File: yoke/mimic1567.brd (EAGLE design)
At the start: 160 x 100 mm, 62 parts, among them J15 JST-VH-5, P1 25 K, P2 10 K, P4 20 K, P5 200, P6 44PINEDGE, Q1 2N3904, Q10 2N2907, Q12 2N3906, Q2 2N3904, Q3 2N3904, Q4 2N3904, Q5 2N3904, Q6 2N3904, Q7 2N3904, Q8 2N2907, Q9 2N3906

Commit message: update netlist
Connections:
- removed net +10V: P6.A
- removed net +5V: P6.F
- removed net -15V: P6.C
- net +50V: now also P6.M; no longer P6.E
- net -10V: now also P6.E
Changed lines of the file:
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@@
 <contactref element="C7" pad="1"/>
 <contactref element="C5" pad="1"/>
+<contactref element="P6" pad="E"/>
 <wire x1="-22.17" y1="113.03" x2="-19.05" y2="124.46" width="0" layer="19" extent="1-1"/>
 <wire x1="-34.29" y1="124.46" x2="-19.05" y2="124.46" width="0" layer="19" extent="1-1"/>
@@
 <wire x1="-54.23" y1="78.74" x2="-35.18" y2="78.74" width="0" layer="19" extent="1-1"/>
 <wire x1="-57.09" y1="66.04" x2="-54.23" y2="78.74" width="0" layer="19" extent="1-1"/>
+<wire x1="-94.3356" y1="50.546" x2="-57.09" y2="66.04" width="0" layer="19" extent="16-16"/>
 <wire x1="-86.86" y1="102.87" x2="-54.23" y2="78.74" width="0" layer="19" extent="1-1"/>
 <wire x1="-103.37" y1="102.87" x2="-86.86" y2="102.87" width="0" layer="19" extent="1-1"/>
@@
 <wire x1="-174.57" y1="-114.3" x2="-181.72" y2="-4.72" width="0" layer="19" extent="1-1"/>
 </signal>
-<signal name="-15V">
-<contactref element="P6" pad="C"/>
-</signal>
-<signal name="+5V">
-<contactref element="P6" pad="F"/>
-</signal>
-<signal name="+10V">
-<contactref element="P6" pad="A"/>
-</signal>
 <signal name="+50V">
-<contactref element="P6" pad="E"/>
 <contactref element="R2" pad="1"/>
 <contactref element="R6" pad="1"/>
 <contactref element="R9" pad="1"/>
 <contactref element="R3" pad="1"/>
+<contactref element="P6" pad="M"/>
+<wire x1="-70.5612" y1="50.546" x2="-100.19" y2="-36.83" width="0" layer="19" extent="16-16"/>
+<wire x1="-65.54" y1="102.87" x2="-70.5612" y2="50.546" width="0" layer="19" extent="16-16"/>
+<wire x1="-82.05" y1="102.87" x2="-65.54" y2="102.87" width="0" layer="19" extent="1-1"/>
 <wire x1="81.42" y1="-106.68" x2="-100.19" y2="-36.83" width="0" layer="19" extent="1-1"/>
-<wire x1="-94.3356" y1="50.546" x2="-100.19" y2="-36.83" width="0" layer="19" extent="16-16"/>
-<wire x1="-82.05" y1="102.87" x2="-94.3356" y2="50.546" width="0" layer="19" extent="16-16"/>
-<wire x1="-65.54" y1="102.87" x2="-82.05" y2="102.87" width="0" layer="19" extent="1-1"/>
 </signal>
 <signal name="N$6">

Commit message: preamplifier card being routed
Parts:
- removed C7: 0.022 uF, keiths:CAP-ZERO-PT-ZERO-22UF-250V-FILM
- removed J15: JST-VH-5, keiths:VHR-5N
- removed P6: 44PINEDGE, keiths:44PINEDGE
- removed Q12: 2N3906, keiths:TO92
- removed R26: 274 K 1%, keiths:R_QUARTERWATT
- added C2: 0.022 uF, keiths:CAP-ZERO-PT-ZERO-22UF-250V-FILM
- added J1: JST-VH-5, keiths:VHR-5N
- added P3: 10 K, keiths:3006P
- added Q11: 2N2907, keiths:TO18
- added R25: 330, keiths:R_ONEWATT
- added R5: 10K, keiths:R_QUARTERWATT
- added R8: 25K, keiths:R_QUARTERWATT
- C1: value 3.3UF 5% -> 3.3uF
- C3, C6: value 0.022 uF -> 0.022uF
- C4: value 3.3UF 5% -> 0.022uF; device keiths:CAP-3-PT-ZERO-3UF-250V-FILM -> keiths:CAP-ZERO-PT-ZERO-22UF-250V-FILM
- C5: value 0.022 uF -> 3.3uF; device keiths:CAP-ZERO-PT-ZERO-22UF-250V-FILM -> keiths:CAP-3-PT-ZERO-3UF-250V-FILM
- P1: value 25 K -> 20K
- P2: value 10 K -> 25 K
- P4: value 20 K -> 200
- P5: value 200 -> 44PINEDGE; device keiths:3006P -> keiths:44PINEDGE
- Q10: value 2N2907 -> 2N3904; device keiths:TO18 -> keiths:TO92
- Q4: value 2N3904 -> 2N2907; device keiths:TO92 -> keiths:TO18
- Q5: value 2N3904 -> 2N3906
- Q8: value 2N2907 -> 2N3906; device keiths:TO18 -> keiths:TO92
- Q9: value 2N3906 -> 2N3904
- R1: value 3.3uF -> 274K; device keiths:R_THREEWATT -> keiths:R_QUARTERWATT
- R10: value 33.2 K 1% -> 274K; device keiths:R_HALFWATT -> keiths:R_QUARTERWATT
- R11: value 4.64K -> 6.81K 1%; device keiths:R_QUARTERWATT -> keiths:R_HALFWATT
- R12: value 2.94K -> 33.2K; device keiths:R_QUARTERWATT -> keiths:R_HALFWATT
- R13: value 3.3 -> 2K; device keiths:R_THREEWATT -> keiths:R_QUARTERWATT
- R14: value 1.96 K 1 % -> 10K; device keiths:R_QUARTERWATT -> keiths:R_HALFWATT
- R15: value 330 5% -> 3.3K; device keiths:R_ONEWATT -> keiths:R_TWOWATT
- R16: value 10 K 5% -> 6.81K
- R17: value 274 K 1% -> 33.2K; device keiths:R_QUARTERWATT -> keiths:R_HALFWATT
- R18: value 1.96 K 1 % -> 2K
- R19: value 1 K 1% -> 10K; device keiths:R_QUARTERWATT -> keiths:R_HALFWATT
- R2: value 3.3K 5% -> 137; device keiths:R_TWOWATT -> keiths:R_QUARTERWATT
- R20: value 137 1% -> 3.3K; device keiths:R_QUARTERWATT -> keiths:R_TWOWATT
- R21: value 1 K 1% -> 3.3; device keiths:R_QUARTERWATT -> keiths:R_THREEWATT
- R22: value 330 5% -> 1K; device keiths:R_ONEWATT -> keiths:R_QUARTERWATT
- R23: value 2 K 1% -> 1K
- R24: value 2 K 1% -> 330; device keiths:R_QUARTERWATT -> keiths:R_ONEWATT
- R3: value 3.3K 5% -> 1.96K; device keiths:R_TWOWATT -> keiths:R_QUARTERWATT
- R4: value 10 K 5% -> 10K; device keiths:R_HALFWATT -> keiths:R_QUARTERWATT
- R6: value 6.81K 1% -> 1.96K; device keiths:R_HALFWATT -> keiths:R_QUARTERWATT
- R7: value 33.2 K 1% -> 25K; device keiths:R_HALFWATT -> keiths:R_QUARTERWATT
- R9: value 6.81K 1% -> 3.3uF; device keiths:R_HALFWATT -> keiths:R_THREEWATT
- moved R21 336.2 mm to (143.5, 33.8), turned to 90 degrees
- moved R14 324.2 mm to (95.2, 58.4), turned to 270 degrees
- moved P4 323.3 mm to (110.5, 101.6), turned to 90 degrees
- moved R19 320.4 mm to (95.2, 41.1), turned to 90 degrees
- moved R24 303.9 mm to (120.7, 22.4), turned to 270 degrees
- moved R23 253.1 mm to (19.1, 22.9), turned to 90 degrees
- moved R2 243.6 mm to (118.1, 87.4), turned to 270 degrees
- moved R20 236.5 mm to (133.3, 22.4), turned to 270 degrees
- moved C3 232.5 mm to (108.0, 55.9), turned to 90 degrees
- moved D7 221.1 mm to (133.3, 65.5), turned to 90 degrees
- moved R9 220.3 mm to (143.5, 86.6), turned to 270 degrees
- moved C1 218.5 mm to (156.2, 87.6)
- moved P5 217.9 mm to (0.00, 57.1), turned to 270 degrees
- moved D2 213.2 mm to (82.5, 82.5), turned to 270 degrees
- moved Q1 208.3 mm to (72.1, 66.0), turned to 45 degrees
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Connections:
- removed net N$13 (its old number): D11.A, D12.C
- removed net N$23: Q5.3
- new net N$37: D12.C, D13.A
- net +50V: now also P5.M, R11.1, R15.1, R16.1, R20.1; no longer P6.M, R2.1, R3.1, R6.1, R9.1
- net -10V: now also C3.1, C4.1, P5.E, Q1.1, Q2.1, Q3.1, Q6.1, Q9.1, R14.2, R19.2, R24.2, R25.2, R6.2; no longer C5.1, C7.1, P6.E, Q1.3, Q2.3, Q4.3, Q6.3, R15.2, R16.2, R18.2, R22.2, R4.2
- net GND: now also J1.P$5, P3.2, P3.3, P5.D, R21.2, R3.2, R4.1, R5.1, R7.1, R8.1, R9.2; no longer J15.P$5, P1.2, P1.3, P6.D, R1.2, R11.1, R12.1, R13.2, R14.2
- net N$10: now also D2.C, D6.A; no longer D14.A, D15.C
- net N$11: now also D1.C, D2.A; no longer D13.A, D14.C
- net N$12: now also D1.A, D4.C; no longer D12.A, D13.C
- net N$14: now also D3.C, D5.A; no longer D10.A, D11.C
- net N$15: now also C2.1, D3.A, Q5.3; no longer C3.1, D10.C, Q9.3
- net N$16: now also Q5.2, Q7.3, R12.2; no longer Q3.1, Q9.2, R7.2
- net N$17: now also R11.2, R12.1; no longer R7.1, R9.2
- net N$19: now also Q1.3, Q10.1, Q7.1; no longer Q3.3, Q5.1, Q7.3
- net N$2: now also J1.P$4, R13.2; no longer J15.P$4, R24.2
- net N$20: now also R16.2, R17.1; no longer R10.1, R6.2
- net N$21: now also Q5.1, Q9.3; no longer Q2.1, Q9.1
- net N$22: now also P4.1, R10.1, R2.2, R3.1; no longer P5.1, R14.1, R20.2, R26.1
- net N$25: now also Q10.3, Q8.2, R17.2; no longer Q12.2, Q7.1, R10.2
- net N$27: now also C5.1, J1.P$2, R18.1; no longer C4.1, J15.P$2, R23.1
- net N$29: now also P3.1, Q1.2, Q2.2, Q2.3, R4.2, R5.2; no longer P2.1, Q5.2, Q6.1, Q6.2, R11.2, R12.2
- net N$3: now also R9.1; no longer R1.1
- net N$30: now also C5.2, R21.1; no longer C4.2, R13.1
- net N$31: now also D16.C, J1.P$1, Q11.1, R20.2; no longer D2.C, J15.P$1, Q10.1, R3.2
- net N$33: now also D15.C, D16.A, Q11.2, R19.1; no longer D1.C, D2.A, Q10.2, R16.1
- net N$34: now also C4.2, Q11.3, R24.1; no longer C7.2, Q10.3, R15.1
- net N$35: now also D14.C, D15.A; no longer D1.A, D3.C
- net N$36: now also D13.C, D14.A; no longer D3.A, D4.C
- net N$38: now also D11.C, D12.A; no longer D5.A, D6.C
- net N$39: now also D10.C, D11.A; no longer D6.A, D7.C
- net N$4: now also P2.1, Q3.2, Q6.2, Q6.3, Q9.2, R7.2, R8.2; no longer P1.1, Q1.1, Q1.2, Q2.2, Q4.2
- net N$40: now also D10.A, Q8.3; no longer D7.A, Q12.3
- net N$43: now also Q10.2, R18.2, R22.2; no longer Q7.2, R21.2, R23.2
- net N$44: now also P4.3, R1.1, R2.1, R6.1; no longer P5.3, R17.1, R18.1, R20.1
- net N$5: now also D7.C, J1.P$3, Q4.1, R15.2; no longer D16.A, J15.P$3, Q8.1, R2.2
- net N$6: now also Q7.2, R13.1, R23.2; no longer Q3.2, R19.2, R24.1
- net N$7: now also C2.2, D6.C, D7.A, Q4.2, R14.1; no longer C3.2, D15.A, D16.C, Q8.2, R4.1
- net N$8: now also C3.2, Q4.3, R25.1; no longer C5.2, Q8.3, R22.1
- net N$9: now also Q3.3, Q8.1; no longer Q12.1, Q4.1
- net W_IN: now also P1.2, P1.3, P5.W, R1.2, R10.2, R22.1; no longer P4.3, P5.2, P6.W, R17.2, R21.1, R26.2
- net Z_IN: now also P1.1, P5.Z, R23.1; no longer P4.1, P6.Z, R19.1
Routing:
- net -10V: track 0.00 -> 252.0 mm
- net GND: track 0.00 -> 241.7 mm
- net W_IN: track 0.00 -> 186.4 mm
- net +50V: track 0.00 -> 166.2 mm
- net N$27: track 0.00 -> 103.5 mm
- net Z_IN: track 0.00 -> 95.3 mm
- net N$6: track 0.00 -> 94.0 mm
- net N$4: track 0.00 -> 84.7 mm
- net N$2: track 0.00 -> 83.2 mm
- net N$15: track 0.00 -> 83.0 mm
- net N$43: track 0.00 -> 79.3 mm
- net N$33: track 0.00 -> 66.8 mm
- net N$31: track 0.00 -> 63.5 mm
- net N$40: track 0.00 -> 62.4 mm
- net N$29: track 0.00 -> 61.2 mm
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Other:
- board size 160 x 100 mm -> 165.1 x 114.3 mm

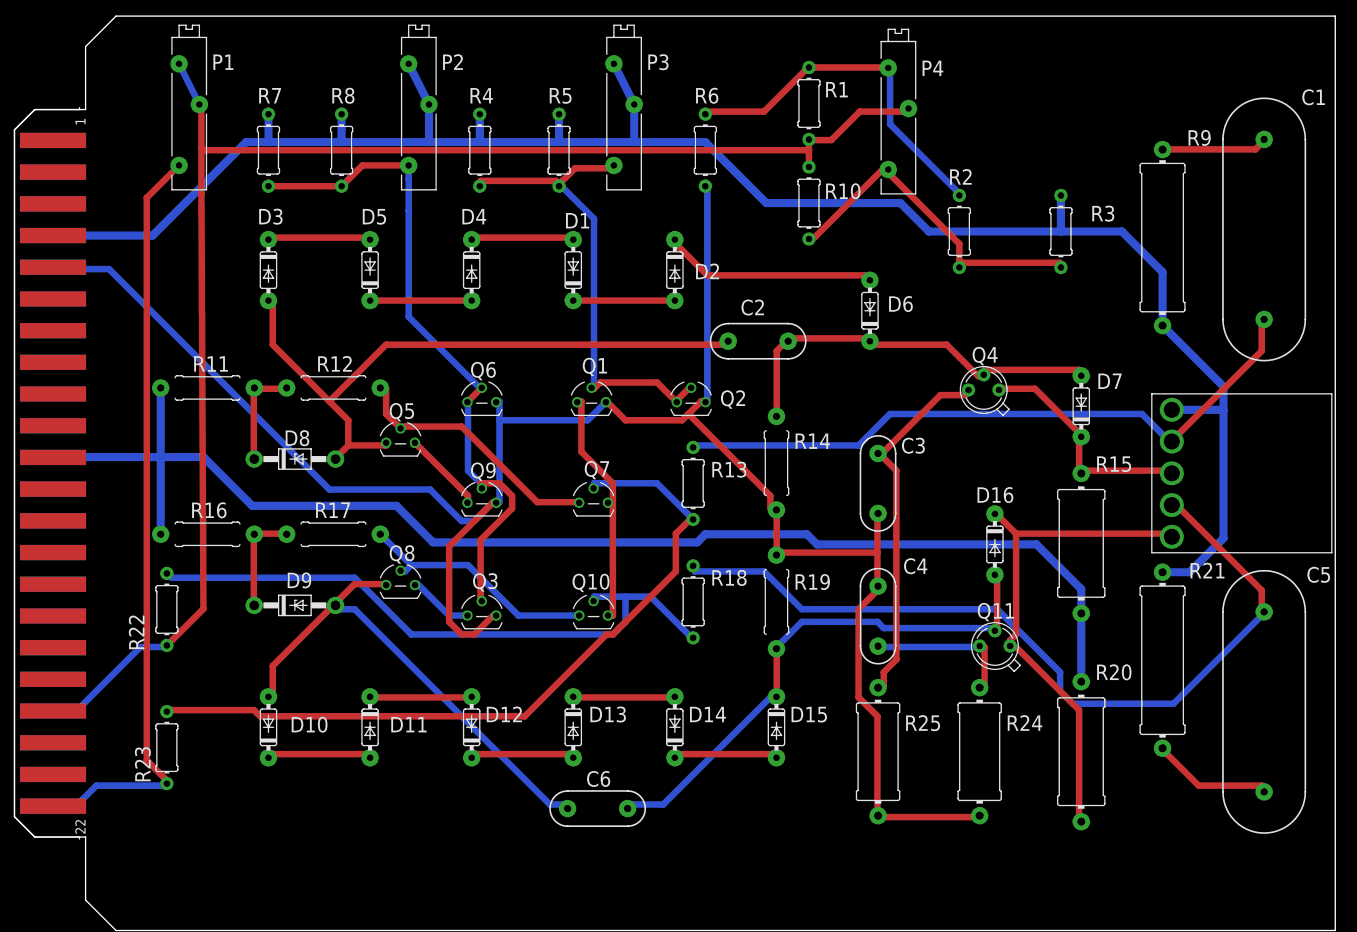
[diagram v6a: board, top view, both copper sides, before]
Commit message: D/A being routed
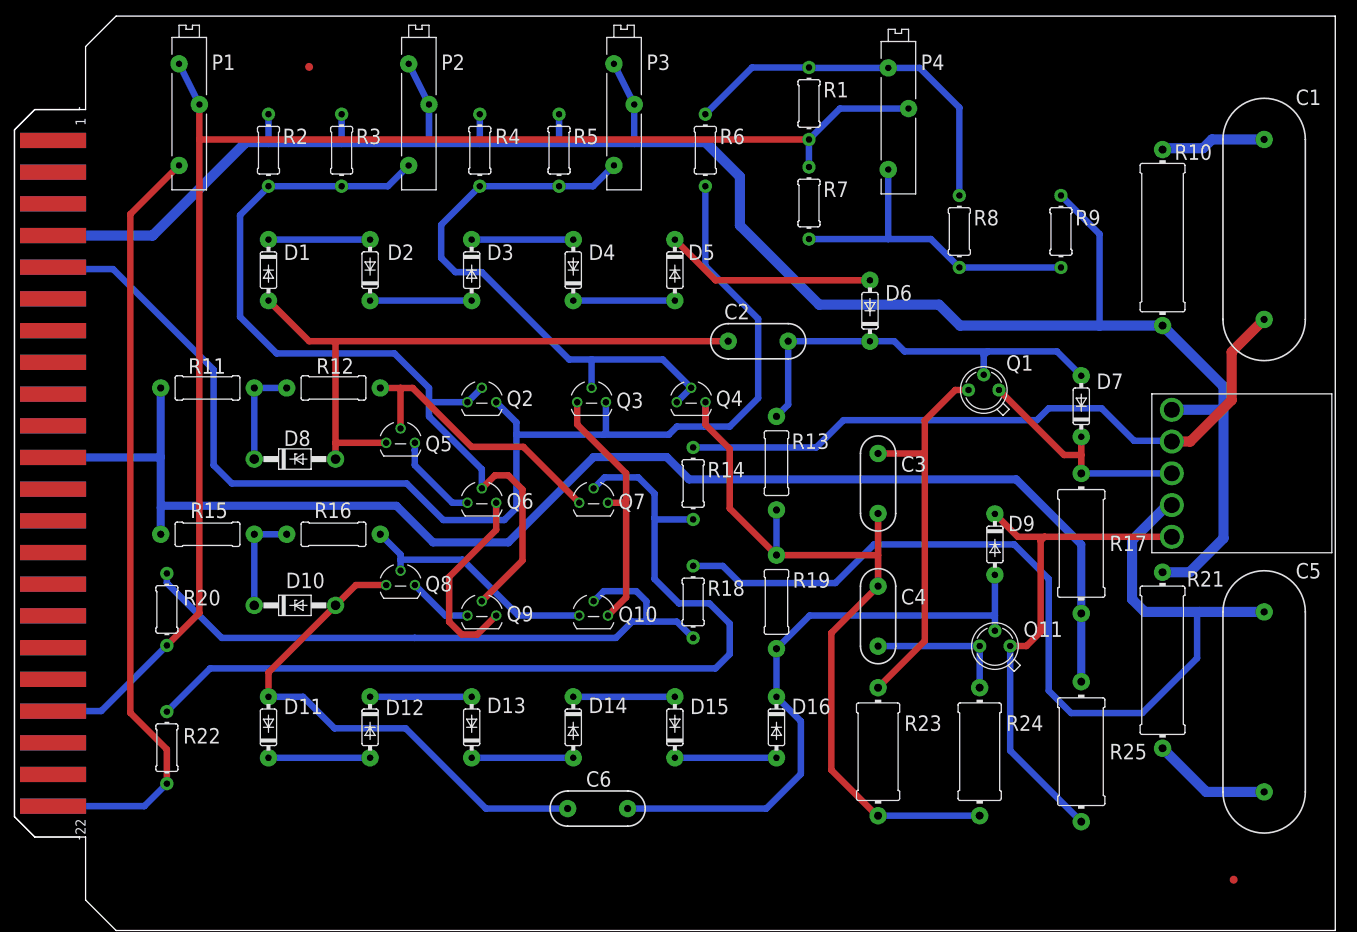
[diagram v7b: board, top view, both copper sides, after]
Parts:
- added U$1, U$2: FIDUCIAL, adafruit:FIDUCIAL_1MM
- D10: value 1N4148 -> 1N4736A; device keiths:DO35-7 -> keiths:DO41
- D9: value 1N4736A -> 1N4148; device keiths:DO41 -> keiths:DO35-7
- Q1: value 2N3904 -> 2N2907; device keiths:TO92 -> keiths:TO18
- Q4: value 2N2907 -> 2N3904; device keiths:TO18 -> keiths:TO92
- R10: value 274K -> 3.3uF; device keiths:R_QUARTERWATT -> keiths:R_THREEWATT
- R11: value 6.81K 1% -> 6.81K
- R13: value 2K -> 10K; device keiths:R_QUARTERWATT -> keiths:R_HALFWATT
- R14: value 10K -> 2K; device keiths:R_HALFWATT -> keiths:R_QUARTERWATT
- R15: value 3.3K -> 6.81K; device keiths:R_TWOWATT -> keiths:R_HALFWATT
- R16: value 6.81K -> 33.2K
- R17: value 33.2K -> 3.3K; device keiths:R_HALFWATT -> keiths:R_TWOWATT
- R2: value 137 -> 25K
- R20: value 3.3K -> 1K; device keiths:R_TWOWATT -> keiths:R_QUARTERWATT
- R23: value 1K -> 330; device keiths:R_QUARTERWATT -> keiths:R_ONEWATT
- R25: value 330 -> 3.3K; device keiths:R_ONEWATT -> keiths:R_TWOWATT
- R3: value 1.96K -> 25K
- R7: value 25K -> 274K
- R8: value 25K -> 137
- R9: value 3.3uF -> 1.96K; device keiths:R_THREEWATT -> keiths:R_QUARTERWATT
- moved R20 115.7 mm to (19.1, 40.1), turned to 90 degrees
- moved R15 109.2 mm to (24.1, 49.5), turned to 0 degrees
- moved R17 93.5 mm to (133.3, 48.4), turned to 90 degrees
- moved R3 90.5 mm to (40.9, 97.5), turned to 270 degrees
- moved R23 88.9 mm to (108.0, 22.4), turned to 270 degrees
- moved D9 87.8 mm to (122.6, 48.3), turned to 270 degrees
- moved R2 87.0 mm to (31.8, 97.5)
- moved R8 77.9 mm to (118.1, 87.4)
- moved R7 67.9 mm to (99.3, 90.9), turned to 90 degrees
- moved Q1 49.0 mm to (121.2, 67.6), turned to 0 degrees
- moved R10 44.4 mm to (143.5, 86.6), turned to 270 degrees
- moved D1 38.1 mm to (31.8, 82.5), turned to 270 degrees
- moved D2 38.1 mm to (44.5, 82.5), turned to 90 degrees
- moved D5 38.1 mm to (82.5, 82.5), turned to 270 degrees
- moved Q4 36.6 mm to (84.6, 66.0), turned to 45 degrees
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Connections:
- removed net N$14 (its old number): D3.C, D5.A
- removed net N$39 (its old number): D10.C, D11.A
- new net N$11: D4.C, D5.A
- new net N$35: D15.C, D16.A
- net +50V: now also R17.1, R25.1; no longer R16.1, R20.1
- net -10V: now also Q4.1, R13.2, R23.2; no longer Q1.1, R14.2, R25.2
- net GND: now also R10.2, R2.1, R3.1; no longer R3.2, R7.1, R8.1
- net N$10: now also D5.C; no longer D2.C
- net N$12: now also D3.C, D4.A; no longer D1.A, D4.C
- net N$13: now also D2.C, D3.A; no longer D4.A, D5.C
- net N$15: now also D1.A; no longer D3.A
- net N$19: now also Q3.3; no longer Q1.3
- net N$2: now also R14.2; no longer R13.2
- net N$20: now also D10.C, R15.2, R16.1; no longer D9.C, R16.2, R17.1
- net N$21: now also Q6.3; no longer Q9.3
- net N$22: now also R7.1, R8.2, R9.1; no longer R10.1, R2.2, R3.1
- net N$25: now also R16.2; no longer R17.2
- net N$29: now also Q3.2, Q4.2, Q4.3; no longer Q1.2, Q2.2, Q2.3
- net N$3: now also R10.1; no longer R9.1
- net N$31: now also D9.C, R25.2; no longer D16.C, R20.2
- net N$33: now also D16.C, D9.A; no longer D15.C, D16.A
- net N$4: now also Q2.2, Q2.3, R2.2, R3.2; no longer Q3.2, Q6.3, R7.2, R8.2
- net N$40: now also D11.A; no longer D9.A
- net N$43: now also R20.2; no longer R22.2
- net N$44: now also R8.1; no longer R2.1
- net N$5: now also Q1.1, R17.2; no longer Q4.1, R15.2
- net N$6: now also R14.1, R22.2; no longer R13.1, R23.2
- net N$7: now also Q1.2, R13.1; no longer Q4.2, R14.1
- net N$8: now also Q1.3, R23.1; no longer Q4.3, R25.1
- net N$9: now also Q9.3; no longer Q3.3
- net W_IN: now also R20.1, R7.2; no longer R10.2, R22.1
- net Z_IN: now also R22.1; no longer R23.1
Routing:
- net -10V: track 252.0 -> 284.9 mm
- net N$4: track 84.7 -> 108.9 mm
- net N$27: track 103.5 -> 123.4 mm
- net N$6: track 94.0 -> 113.5 mm
- net GND: track 241.7 -> 255.2 mm
- net N$39 (its old number): track 13.1 -> 0.00 mm
- net N$14 (its old number): track 12.8 -> 0.00 mm
- net N$35: track 0.00 -> 12.7 mm
- net N$11: track 0.00 -> 12.7 mm
- net N$29: track 61.2 -> 72.8 mm
- net N$33: track 66.8 -> 76.4 mm
- net +50V: track 166.2 -> 174.9 mm
- net N$16: track 32.7 -> 35.9 mm
- net N$40: track 62.4 -> 65.5 mm
- net N$8: track 46.0 -> 48.7 mm
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
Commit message: end of day
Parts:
- added R26, R27: 1.2K, keiths:R_FIVEWATT
- added R28: 1K, keiths:R_QUARTERWATT
- added R29, R30: 330, keiths:R_ONEWATT
- C2: value 0.022 uF -> 3.3uF; device keiths:CAP-ZERO-PT-ZERO-22UF-250V-FILM -> keiths:CAP-3-PT-ZERO-3UF-250V-FILM
- C3: value 0.022uF -> 0.022 uF
- C5: value 3.3uF -> 0.022uF; device keiths:CAP-3-PT-ZERO-3UF-250V-FILM -> keiths:CAP-ZERO-PT-ZERO-22UF-250V-FILM
- P3: value 10 K -> 5K
- R10: value 3.3uF -> 1.96K; device keiths:R_THREEWATT -> keiths:R_QUARTERWATT
- R11: value 6.81K -> 3.3; device keiths:R_HALFWATT -> keiths:0309/12
- R12: value 33.2K -> 100; device keiths:R_HALFWATT -> keiths:R_QUARTERWATT
- R13: value 10K -> 22; device keiths:R_HALFWATT -> keiths:R_QUARTERWATT
- R14: value 2K -> 22
- R17: value 3.3K -> 100; device keiths:R_TWOWATT -> keiths:R_QUARTERWATT
- R18: value 2K -> 10K; device keiths:R_QUARTERWATT -> keiths:R_HALFWATT
- R19: value 10K -> 2K; device keiths:R_HALFWATT -> keiths:R_QUARTERWATT
- R2, R3: value 25K -> 20K
- R20: value 1K -> 6.81K; device keiths:R_QUARTERWATT -> keiths:R_HALFWATT
- R21: value 3.3 -> 33.2K; device keiths:R_THREEWATT -> keiths:R_HALFWATT
- R22: value 1K -> 100
- R23: value 330 -> 2K; device keiths:R_ONEWATT -> keiths:R_QUARTERWATT
- R24: value 330 -> 10K; device keiths:R_ONEWATT -> keiths:R_HALFWATT
- R25: value 3.3K -> 1K; device keiths:R_TWOWATT -> keiths:R_QUARTERWATT
- R4: value 10K -> 3.9K
- R5: value 10K -> 4.7K
- R6: value 1.96K -> 274K
- R7: value 274K -> 137
- R8: value 137 -> 1.96K
- R9: value 1.96K -> 3.3; device keiths:R_QUARTERWATT -> keiths:0309/12
- moved R11 127.0 mm to (151.0, 73.8), turned to 180 degrees
- moved R25 115.7 mm to (19.1, 40.1), turned to 90 degrees
- moved R21 104.8 mm to (39.9, 49.5), turned to 0 degrees
- moved R17 67.6 mm to (66.5, 58.9)
- moved R22 51.2 mm to (65.8, 43.9)
- moved C2 50.7 mm to (139.7, 93.2)
- moved C5 49.4 mm to (108.0, 39.3)
- moved R8 29.4 mm to (88.8, 89.4), turned to 180 degrees
- moved R24 29.2 mm to (98.3, 41.1), turned to 90 degrees
- moved R23 28.1 mm to (88.3, 42.4), turned to 180 degrees
- moved R13 26.5 mm to (72.1, 71.4), turned to 180 degrees
- moved C1 25.8 mm to (139.7, 107.4), turned to 0 degrees
- moved C6 24.8 mm to (87.6, 35.2)
- moved R18 22.0 mm to (98.3, 58.4)
- moved R10 21.4 mm to (122.9, 80.8)
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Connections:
- new net N$1: Q4.1, R14.1
- new net N$18: Q3.1, R13.1
- new net N$23: Q9.1, R22.1
- new net N$24: Q6.1, R17.1
- new net N$26: Q2.1, R12.1
- net +50V: now also R20.1, R26.1, R27.1; no longer R11.1, R17.1, R25.1
- net -10V: now also C5.1, R10.2, R12.2, R14.2, R17.2, R18.2, R22.2, R29.2, R30.2; no longer C3.1, Q2.1, Q3.1, Q4.1, Q6.1, Q9.1, R19.2, R23.2, R6.2
- net GND: now also R11.2, R8.2; no longer R10.2, R21.2
- net N$15: now also C3.1; no longer C2.1
- net N$16: now also R16.2; no longer R12.2
- net N$17: now also R15.2, R16.1; no longer R11.2, R12.1
- net N$2: now also C2.1, R19.2; no longer C1.1, R14.2
- net N$20: now also R20.2, R21.1; no longer R15.2, R16.1
- net N$22: now also R6.1, R7.2, R8.1; no longer R7.1, R8.2, R9.1
- net N$25: now also R21.2; no longer R16.2
- net N$27: now also C1.1, R23.1; no longer C5.1, R18.1
- net N$3: now also C2.2, R9.1; no longer C1.2, R10.1
- net N$30: now also C1.2, R11.1; no longer C5.2, R21.1
- net N$31: now also R27.2; no longer R25.2
- net N$33: now also R24.1; no longer R19.1
- net N$34: now also C5.2, R30.1; no longer C4.2, R24.1
- net N$43: now also R23.2, R25.2; no longer R18.2, R20.2
- net N$44: now also R10.1, R7.1; no longer R6.1, R8.1
- net N$5: now also R26.2; no longer R17.2
- net N$6: now also R19.1, R28.2; no longer R14.1, R22.2
- net N$7: now also C3.2, R18.1; no longer C2.2, R13.1
- net N$8: now also C4.2, R29.1; no longer C3.2, R23.1
- net W_IN: now also R25.1, R6.2; no longer R20.1, R7.2
- net Z_IN: now also R28.1; no longer R22.1
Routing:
- net N$27: track 123.4 -> 155.3 mm
- net N$33: track 76.4 -> 45.9 mm
- net -10V: track 284.9 -> 315.4 mm
- net N$2: track 85.0 -> 108.7 mm
- net N$30: track 15.0 -> 38.2 mm
- net N$5: track 29.6 -> 52.0 mm
- net N$15: track 80.7 -> 98.5 mm
- net N$40: track 65.5 -> 79.8 mm
- net +50V: track 174.9 -> 188.5 mm
- net N$22: track 41.7 -> 33.0 mm
- net GND: track 255.2 -> 246.7 mm
- net N$29: track 72.8 -> 80.1 mm
- net N$44: track 47.2 -> 40.3 mm
- net N$24: track 0.00 -> 6.73 mm
- net N$26: track 0.00 -> 6.45 mm
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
